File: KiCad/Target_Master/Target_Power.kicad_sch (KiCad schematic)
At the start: 8 parts, among them SW1 SW_SPST, U1 AMS1117-5

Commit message: Finalized schematics
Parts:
- removed BT1: ???, symbol Device:Battery_Cell
- removed C1, C2: 10uF, Capacitor_SMD:C_0805_2012Metric_Pad1.18x1.45mm_HandSolder, symbol Device:C_Polarized_Small_US
- removed C3: 1uF, Capacitor_SMD:C_0805_2012Metric_Pad1.18x1.45mm_HandSolder, symbol Device:C_Small
- removed SW1: SW_SPST, symbol Switch:SW_SPST
- removed U1: AMS1117-5, Package_TO_SOT_SMD:SOT-223-3_TabPin2, symbol Regulator_Linear:AMS1117-3.3
- added C11: 0.1uF, symbol Device:C_Small
- added C3, C9: 220uF, symbol Device:C_Polarized_Small_US
- added DC_Supply: +5V, symbol Device:Battery_Cell
- D1: value LED -> +5V; footprint LED_SMD:LED_0805_2012Metric_Pad1.15x1.40mm_HandSolder -> (none)
- R1: value 2.2KΩ -> 4.7kΩ; footprint Resistor_SMD:R_0805_2012Metric_Pad1.20x1.40mm_HandSolder -> (none)
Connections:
- net +5V: now also C11.1, C3.1, C9.1, DC_Supply.1 (+)
- net GND: now reaches R1.1
- net GND: now also C11.2, C3.2, C9.2, DC_Supply.2 (-)

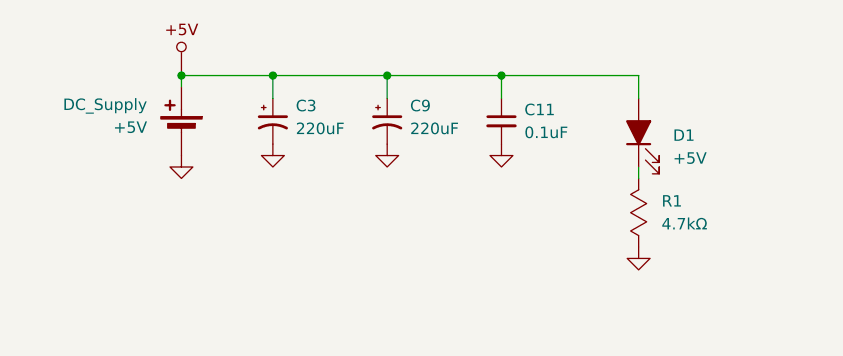
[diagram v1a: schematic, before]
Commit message: Master PCB design, Slave board logos
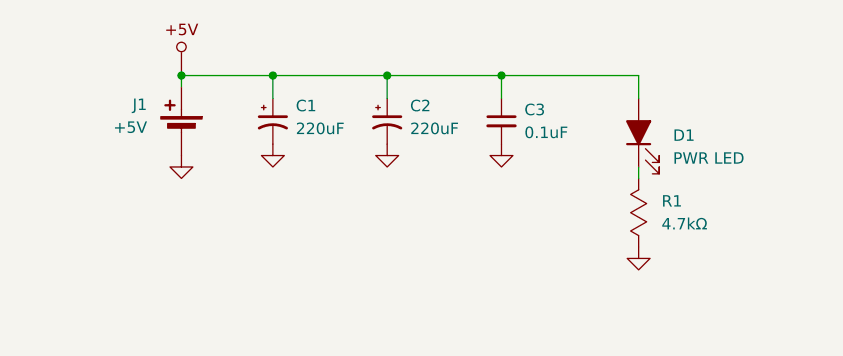
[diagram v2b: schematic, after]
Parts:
- C1: renamed from C3; footprint (none) -> Capacitor_THT:CP_Radial_D6.3mm_P2.50mm
- C2: renamed from C9; footprint (none) -> Capacitor_THT:CP_Radial_D6.3mm_P2.50mm
- C3: renamed from C11; footprint (none) -> Capacitor_SMD:C_0805_2012Metric_Pad1.18x1.45mm_HandSolder
- D1: value +5V -> PWR LED; footprint (none) -> LED_SMD:LED_0805_2012Metric_Pad1.15x1.40mm_HandSolder
- J1: renamed from DC_Supply; footprint (none) -> 0_AKeller_Footprints:AMASS_XT30PW-M_1x02_P2.50mm_Horizontal
- R1: footprint (none) -> Resistor_SMD:R_0805_2012Metric_Pad1.20x1.40mm_HandSolder
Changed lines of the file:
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@@
 		(dnp no)
 		(fields_autoplaced yes)
-		(property "Reference" "#PWR012"
+		(property "Reference" "#PWR01"
 			(at 123.19 104.14 0)
 			(effects
@@
 			(project "Target"
 				(path "/b95a4fbb-e866-40f1-8b06-3d5c3eea26d9/0e3f4d82-cc09-4ba7-85db-e6aa39e63df5"
-					(reference "#PWR012")
+					(reference "#PWR01")
 					(unit 1)
 				)
@@
 			)
 		)
-		(property "Value" "+5V"
+		(property "Value" "PWR LED"
 			(at 167.64 99.3774 90)
 			(effects
@@
 			)
 		)
-		(property "Footprint" ""
+		(property "Footprint" "LED_SMD:LED_0805_2012Metric_Pad1.15x1.40mm_HandSolder"
 			(at 163.83 96.52 0)
 			(effects
@@
 		(dnp no)
 		(fields_autoplaced yes)
-		(property "Reference" "C3"
+		(property "Reference" "C1"
 			(at 125.73 93.5481 0)
 			(effects
@@
 			)
 		)
-		(property "Footprint" ""
+		(property "Footprint" "Capacitor_THT:CP_Radial_D6.3mm_P2.50mm"
 			(at 123.19 95.25 0)
 			(effects
@@
 			(project "Target"
 				(path "/b95a4fbb-e866-40f1-8b06-3d5c3eea26d9/0e3f4d82-cc09-4ba7-85db-e6aa39e63df5"
-					(reference "C3")
+					(reference "C1")
 					(unit 1)
 				)
@@
 		(dnp no)
 		(fields_autoplaced yes)
-		(property "Reference" "C11"
+		(property "Reference" "C3"
 			(at 151.13 93.9862 0)
 			(effects
@@
 			)
 		)
-		(property "Footprint" ""
+		(property "Footprint" "Capacitor_SMD:C_0805_2012Metric_Pad1.18x1.45mm_HandSolder"
 			(at 148.59 95.25 0)
 			(effects
@@
 			(project "Target"
 				(path "/b95a4fbb-e866-40f1-8b06-3d5c3eea26d9/0e3f4d82-cc09-4ba7-85db-e6aa39e63df5"
-					(reference "C11")
+					(reference "C3")
 					(unit 1)
 				)
@@
 		(dnp no)
 		(fields_autoplaced yes)
-		(property "Reference" "#PWR010"
+		(property "Reference" "#PWR03"
 			(at 148.59 104.14 0)
 			(effects
@@
 			(project "Target"
 				(path "/b95a4fbb-e866-40f1-8b06-3d5c3eea26d9/0e3f4d82-cc09-4ba7-85db-e6aa39e63df5"
-					(reference "#PWR010")
+					(reference "#PWR03")
 					(unit 1)
 				)
@@
 		(dnp no)
 		(fields_autoplaced yes)
-		(property "Reference" "#PWR011"
+		(property "Reference" "#PWR02"
 			(at 135.89 104.14 0)
 			(effects
@@
 			(project "Target"
 				(path "/b95a4fbb-e866-40f1-8b06-3d5c3eea26d9/0e3f4d82-cc09-4ba7-85db-e6aa39e63df5"
-					(reference "#PWR011")
+					(reference "#PWR02")
 					(unit 1)
 				)
@@
 		(dnp no)
 		(fields_autoplaced yes)
-		(property "Reference" "#PWR013"
+		(property "Reference" "#PWR04"
 			(at 113.03 105.41 0)
 			(effects
@@
 			(project "Target"
 				(path "/b95a4fbb-e866-40f1-8b06-3d5c3eea26d9/0e3f4d82-cc09-4ba7-85db-e6aa39e63df5"
-					(reference "#PWR013")
+					(reference "#PWR04")
 					(unit 1)
 				)
@@
 		(dnp no)
 		(fields_autoplaced yes)
-		(property "Reference" "#PWR02"
+		(property "Reference" "#PWR05"
 			(at 163.83 115.57 0)
 			(effects
@@
 			(project "Target"
 				(path "/b95a4fbb-e866-40f1-8b06-3d5c3eea26d9/0e3f4d82-cc09-4ba7-85db-e6aa39e63df5"
-					(reference "#PWR02")
+					(reference "#PWR05")
 					(unit 1)
 				)
@@
 		(on_board yes)
 		(dnp no)
-		(property "Reference" "DC_Supply"
+		(property "Reference" "J1"
 			(at 109.22 93.4084 0)
 			(effects
@@
 			)
 		)
-		(property "Footprint" ""
+		(property "Footprint" "0_AKeller_Footprints:AMASS_XT30PW-M_1x02_P2.50mm_Horizontal"
 			(at 113.03 94.996 90)
 			(effects
@@
 			(project "Target"
 				(path "/b95a4fbb-e866-40f1-8b06-3d5c3eea26d9/0e3f4d82-cc09-4ba7-85db-e6aa39e63df5"
-					(reference "DC_Supply")
+					(reference "J1")
 					(unit 1)
 				)
@@
 		(dnp no)
 		(fields_autoplaced yes)
-		(property "Reference" "C9"
+		(property "Reference" "C2"
 			(at 138.43 93.5481 0)
 			(effects
@@
 			)
 		)
-		(property "Footprint" ""
+		(property "Footprint" "Capacitor_THT:CP_Radial_D6.3mm_P2.50mm"
 			(at 135.89 95.25 0)
 			(effects
@@
 			(project "Target"
 				(path "/b95a4fbb-e866-40f1-8b06-3d5c3eea26d9/0e3f4d82-cc09-4ba7-85db-e6aa39e63df5"
-					(reference "C9")
+					(reference "C2")
 					(unit 1)
 				)
@@
 		(dnp no)
 		(fields_autoplaced yes)
-		(property "Reference" "+5V08"
+		(property "Reference" "#+5V01"
 			(at 113.03 85.09 0)
 			(effects
@@
 			(project "Target"
 				(path "/b95a4fbb-e866-40f1-8b06-3d5c3eea26d9/0e3f4d82-cc09-4ba7-85db-e6aa39e63df5"
-					(reference "+5V08")
+					(reference "#+5V01")
 					(unit 1)
 				)
@@
 			)
 		)
-		(property "Footprint" ""
+		(property "Footprint" "Resistor_SMD:R_0805_2012Metric_Pad1.20x1.40mm_HandSolder"
 			(at 163.83 104.648 0)
 			(effects

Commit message: Master board silkscreen and gerber files
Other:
- title: Power -> Laser Arcade Master
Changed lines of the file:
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@@
 	(paper "A")
 	(title_block
-		(title "Power")
-		(date "2025-04-04")
+		(title "Laser Arcade Master")
+		(date "2025-04-17")
 		(rev "A")
 		(company "Idaho State University")
